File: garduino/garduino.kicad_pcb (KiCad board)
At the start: 2 copper layers, 65 x 56 mm, 62 parts, among them J1 Hum1, J10 OUT6, J11 DIN1, J12 OUT5, J13 OUT4, J14 OUT3, J15 isp, J16 OUT2, J17 OUT1, J18 RPi, J2 Hum2, J3 Hum3, J4 Hum4, J5 Hum5, J6 Hum6, J7 RL0, J8 OUT7, J9 DIN0, Q1 Q_PNP_BCE, Q2 Q_PNP_BCE, Q3 Q_PNP_BCE, Q4 Q_PNP_BCE, Q5 Q_PNP_BCE, Q6 Q_PNP_BCE, Q7 Q_PNP_BCE, Q8 Q_PNP_BCE, SW1 reset, U1 TPIC6595, U2 ATmega328-AU, U3 LM7805_TO220

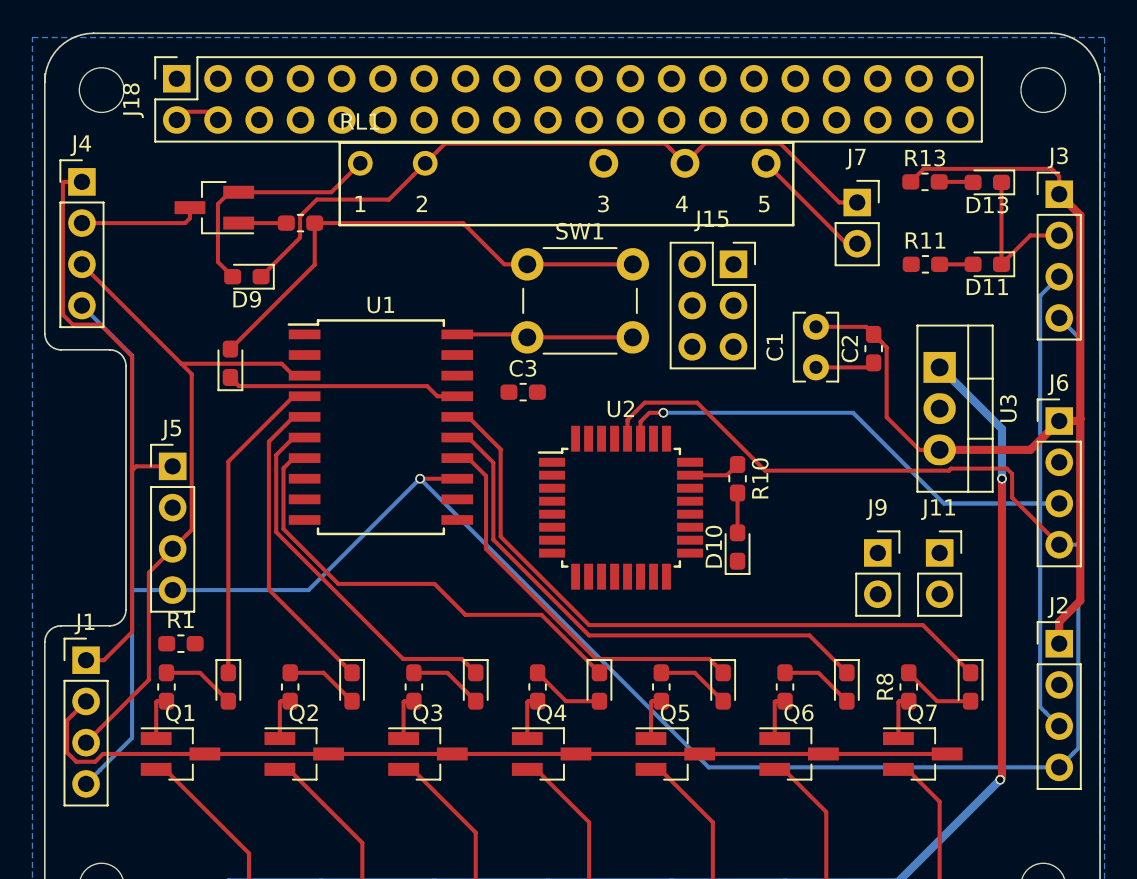
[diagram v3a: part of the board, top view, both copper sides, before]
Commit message: Add capsensor, humidity sensor p3, garduino with avr
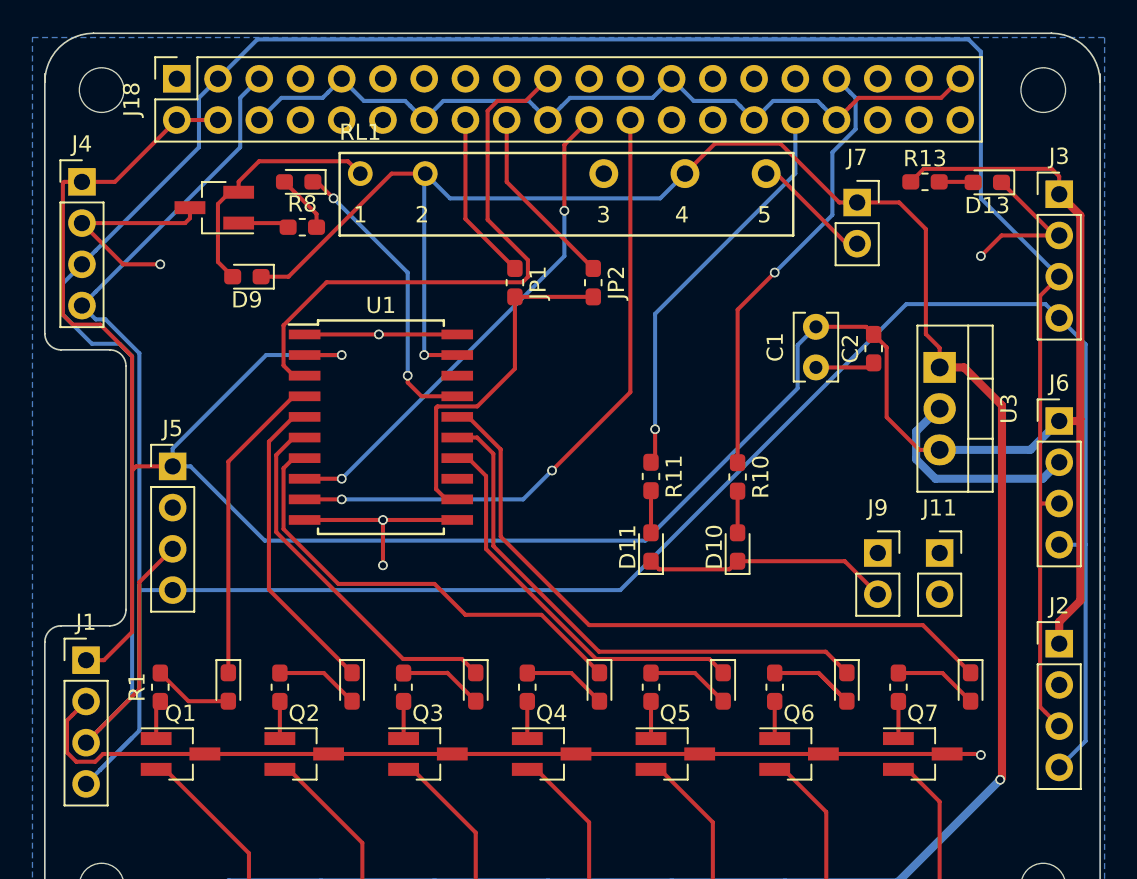
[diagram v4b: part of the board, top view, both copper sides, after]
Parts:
- removed C3: 100nF, Capacitor_SMD:C_0603_1608Metric_Pad1.05x0.95mm_HandSolder
- removed J15: isp, Connector_PinSocket_2.54mm:PinSocket_2x03_P2.54mm_Vertical
- removed R9: 10k, Resistor_SMD:R_0603_1608Metric_Pad1.05x0.95mm_HandSolder
- removed SW1: reset, Button_Switch_THT:SW_PUSH_6mm_H4.3mm
- removed U2: ATmega328-AU, Package_QFP:TQFP-32_7x7mm_P0.8mm
- added JP1: BCM23, Resistor_SMD:R_0603_1608Metric_Pad1.05x0.95mm_HandSolder, F.Cu at (118.6, 104.0)
- added JP2: BCM24, Resistor_SMD:R_0603_1608Metric_Pad1.05x0.95mm_HandSolder, F.Cu at (123.4, 104.0)
- moved R8 46.9 mm to (105.5, 100.6), turned to 0 degrees
- moved D11 27.1 mm to (127.0, 120.3), turned to 90 degrees
- moved R11 21.4 mm to (127.0, 115.9), turned to 270 degrees
- moved D8 11.9 mm to (105.3, 97.8), turned to 180 degrees
- moved R7 6.99 mm to (142.2, 128.9)
- moved R2 6.99 mm to (104.1, 128.9)
- moved R3 6.99 mm to (111.8, 128.9)
- moved R4 6.99 mm to (119.4, 128.9)
- moved R5 6.99 mm to (127.0, 128.9)
- moved R6 6.99 mm to (134.6, 128.9)
- moved R1 2.97 mm to (96.8, 128.9), turned to 90 degrees
- moved RL1 0.63 mm to (109.1, 97.3)
- moved R10 0.11 mm to (132.3, 116.0)
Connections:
- net /MOSI renamed /SPI0_MOSI
- J18 pad 16: (no net) -> /BCM23
- J18 pad 18: (no net) -> /BCM24
- J18 pad 2: /5v -> +5V
- J18 pad 21: /MISO -> (no net)
- J18 pad 22: (no net) -> /BCM25
- J18 pad 24: (no net) -> /SPI0_CE0
- J18 pad 3: /RESET -> /SDA
- J18 pad 32: (no net) -> /PWM0
- J18 pad 33: (no net) -> /PWM1
- J18 pad 4: /5v -> +5V
- J18 pad 5: (no net) -> /SCL
- J5 pad 3: (no net) -> /SDA
- R10 pad 1: /LED1 -> /PWM1
- R11 pad 1: /LED2 -> /PWM0
- U1 pad 13: /SCK -> (no net)
- U1 pad 8: /RESET -> /BCM25
- U1 pad 9: /G# -> /SPI0_CE0
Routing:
- net /SCK: track 131.4 -> 0.00 mm, vias 1 -> 0
- net /SCL: track 32.8 -> 148.0 mm
- net /SDA: track 58.0 -> 156.9 mm, vias 1 -> 0
- net GND: track 89.6 -> 188.3 mm, vias 0 -> 6
- net +5V: track 100.0 -> 174.7 mm, vias 0 -> 1
- net /SPI0_CE0: track 0.00 -> 39.6 mm, vias 0 -> 2
- net /BCM25: track 0.00 -> 30.7 mm, vias 0 -> 2
- net +12V: track 130.4 -> 157.8 mm
- net /PWM1: track 0.00 -> 27.1 mm, vias 0 -> 1
- net /PWM0: track 0.00 -> 24.8 mm, vias 0 -> 1
- net /RCLK: track 0.00 -> 21.7 mm
- net Net-(C3-Pad1): track 20.2 -> 0.00 mm
- net /BCM24: track 0.00 -> 11.4 mm
- net /BCM23: track 0.00 -> 10.4 mm
- net /SPI0_MOSI: track 42.9 -> 36.1 mm
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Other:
- board text removed: "Camera Flex Slot (Optional)"

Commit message: Garduino with FETs
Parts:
- removed D1, D10, D11, D13, D2, D3, D4, D5, D6, D7: LED, LED_SMD:LED_0603_1608Metric_Pad1.05x0.95mm_HandSolder
- removed the D8 at (105.3, 97.8)
- removed the J14 at (113.0, 142.2)
- removed JP1: BCM23, Resistor_SMD:R_0603_1608Metric_Pad1.05x0.95mm_HandSolder
- removed JP2: BCM24, Resistor_SMD:R_0603_1608Metric_Pad1.05x0.95mm_HandSolder
- removed R1, R3, R4, R5, R6, R7: 1k, Resistor_SMD:R_0603_1608Metric_Pad1.05x0.95mm_HandSolder
- removed R2: 10k, Resistor_SMD:R_0603_1608Metric_Pad1.05x0.95mm_HandSolder
- removed U1: TPIC6595, Package_SO:SOIC-20W_7.5x12.8mm_P1.27mm
- removed U3: LM7805_TO220, Package_TO_SOT_THT:TO-220-3_Vertical
- added C1: 100n, Capacitor_SMD:C_0603_1608Metric_Pad1.05x0.95mm_HandSolder, F.Cu at (123.3, 111.8)
- added C2: 22pF, Capacitor_SMD:C_0603_1608Metric_Pad1.05x0.95mm_HandSolder, F.Cu at (119.7, 111.8)
- added C3: 22pF, Capacitor_SMD:C_0603_1608Metric_Pad1.05x0.95mm_HandSolder, F.Cu at (116.2, 111.8)
- added D9: LED, LED_SMD:LED_0603_1608Metric_Pad1.05x0.95mm_HandSolder, F.Cu at (147.1, 142.6)
- added J15: OUT3, Connector_PinSocket_2.54mm:PinSocket_1x02_P2.54mm_Vertical, F.Cu at (114.6, 142.0)
- added J17: OUT2, Connector_PinSocket_2.54mm:PinSocket_1x02_P2.54mm_Vertical, F.Cu at (107.4, 142.0)
- added J9: ADC6, Connector_PinHeader_2.54mm:PinHeader_1x03_P2.54mm_Vertical, F.Cu at (147.6, 119.6)
- added Q10: BSS138, Package_TO_SOT_SMD:SOT-23, F.Cu at (93.9, 101.7)
- added Q11: BSS138, Package_TO_SOT_SMD:SOT-23, F.Cu at (133.1, 114.3)
- added Q12: NCV8403, Package_TO_SOT_SMD:TO-252-2, F.Cu at (104.0, 105.5)
- added Q9: BSS138, Package_TO_SOT_SMD:SOT-23, B.Cu at (123.3, 103.1)
- added R12: 10k, Resistor_SMD:R_0603_1608Metric_Pad1.05x0.95mm_HandSolder, F.Cu at (93.8, 98.4)
- added R14: 1k, Resistor_SMD:R_0603_1608Metric_Pad1.05x0.95mm_HandSolder, F.Cu at (147.1, 138.9)
- added R15: 10k, Resistor_SMD:R_0603_1608Metric_Pad1.05x0.95mm_HandSolder, F.Cu at (136.0, 114.3)
- added R16: 10k, Resistor_SMD:R_0603_1608Metric_Pad1.05x0.95mm_HandSolder, F.Cu at (130.2, 114.3)
- added R17: 10k, Resistor_SMD:R_0603_1608Metric_Pad1.05x0.95mm_HandSolder, B.Cu at (130.7, 106.6)
- added R9: 10k, Resistor_SMD:R_0603_1608Metric_Pad1.05x0.95mm_HandSolder, B.Cu at (118.1, 103.1)
- added SW1: SW_DIP_x01, Button_Switch_SMD:SW_SPST_B3S-1000, F.Cu at (130.5, 106.6)
- added U2: ATmega328P-AU, Package_QFP:TQFP-32_7x7mm_P0.8mm, F.Cu at (120.4, 118.5)
- added Y1: Crystal, Crystal:Crystal_HC18-U_Vertical, F.Cu at (121.9, 108.0)
- D8: renamed from D9; moved to B.Cu
- J1: value Hum1 -> ADC1; footprint Connector_PinHeader_2.54mm:PinHeader_1x04_P2.54mm_Vertical -> Connector_PinHeader_2.54mm:PinHeader_1x03_P2.54mm_Vertical
- J11: value DIN1 -> ADC7; footprint Connector_PinSocket_2.54mm:PinSocket_1x02_P2.54mm_Vertical -> Connector_PinHeader_2.54mm:PinHeader_1x03_P2.54mm_Vertical
- J14: renamed from J9; value DIN0 -> DIN
- J16: value OUT2 -> 12v
- J2: value Hum2 -> ADC2; footprint Connector_PinHeader_2.54mm:PinHeader_1x04_P2.54mm_Vertical -> Connector_PinHeader_2.54mm:PinHeader_1x03_P2.54mm_Vertical
- J3: value Hum3 -> ADC3; footprint Connector_PinHeader_2.54mm:PinHeader_1x04_P2.54mm_Vertical -> Connector_PinHeader_2.54mm:PinHeader_1x03_P2.54mm_Vertical
- J4: value Hum4 -> Max7219; footprint Connector_PinHeader_2.54mm:PinHeader_1x04_P2.54mm_Vertical -> Connector_PinHeader_2.54mm:PinHeader_1x05_P2.54mm_Vertical
- J5: value Hum5 -> ADC4; footprint Connector_PinHeader_2.54mm:PinHeader_1x04_P2.54mm_Vertical -> Connector_PinHeader_2.54mm:PinHeader_1x03_P2.54mm_Vertical
- J6: value Hum6 -> ADC5; footprint Connector_PinHeader_2.54mm:PinHeader_1x04_P2.54mm_Vertical -> Connector_PinHeader_2.54mm:PinHeader_1x03_P2.54mm_Vertical
- J7: value RL0 -> OUT8
- Q1, Q2, Q3, Q4, Q5, Q6, Q7: value Q_PNP_BCE -> NCV8403; footprint Package_TO_SOT_SMD:SOT-23_Handsoldering -> Package_TO_SOT_SMD:TO-252-2
- Q8: value Q_PNP_BCE -> BSS138; footprint Package_TO_SOT_SMD:SOT-23_Handsoldering -> Package_TO_SOT_SMD:SOT-23; moved to B.Cu
- R10, R11, R8: value 1k -> 10k; moved to B.Cu
- R13: value 1k -> 10k
- moved J1 66.1 mm to (151.9, 98.8)
- moved J5 56.3 mm to (151.9, 130.0)
- moved R13 50.5 mm to (93.8, 104.5)
- moved J14 22.8 mm to (147.6, 98.8)
- moved J3 21.1 mm to (151.9, 119.6)
- moved J4 18.8 mm to (104.4, 111.9)
- moved J6 18.1 mm to (147.6, 130.0)
- moved J16 17.8 mm to (92.2, 131.8), turned to 0 degrees
- moved R10 17.4 mm to (120.5, 103.1)
- moved J2 17.0 mm to (151.9, 109.2)
- moved Q8 15.6 mm to (115.2, 103.1), turned to 0 degrees
- moved R11 12.8 mm to (126.2, 103.1)
- moved J11 11.8 mm to (147.6, 109.2)
- moved D8 9.67 mm to (111.0, 99.8)
- moved R8 7.32 mm to (112.4, 103.1), turned to 270 degrees
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- renumbered C1 to C4, C2 to C5, J17 to J18, J18 to J19
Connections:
- J1 pad 1: +5V -> GND
- J1 pad 2: GND -> +5V
- J1 pad 3: /SDA -> /PC5
- J11 pad 1: (no net) -> GND
- J11 pad 2: GND -> +5V
- J14 pad 1: (no net) -> GND
- J14 pad 2: GND -> /PD4
- J16 pad 1: +12V -> GND
- J16 pad 2: /OUT1 -> +12V
- J19 pad 1: (no net) -> +3V3
- J19 pad 16: /BCM23 -> (no net)
- J19 pad 18: /BCM24 -> (no net)
- J19 pad 21: (no net) -> /SPI0_MISO
- J19 pad 23: (no net) -> /SPI0_SCLK
- J19 pad 24: /SPI0_CE0 -> (no net)
- J19 pad 3: /SDA -> (no net)
- J19 pad 32: /PWM0 -> (no net)
- J19 pad 33: /PWM1 -> (no net)
- J19 pad 5: /SCL -> (no net)
- J2 pad 1: +5V -> GND
- J2 pad 2: (no net) -> +5V
- J2 pad 3: /SDA -> /PC3
- J3 pad 1: +5V -> GND
- J3 pad 2: GND -> +5V
- J3 pad 3: /SDA -> /PC2
- J4 pad 3: /SDA -> /MAXDIN
- J4 pad 4: /SCL -> /MAXCS
- J5 pad 1: +5V -> GND
- J5 pad 2: GND -> +5V
- J5 pad 3: /SDA -> /ADC7
- J6 pad 1: +5V -> GND
- J6 pad 2: GND -> +5V
- J6 pad 3: /SDA -> /ADC6
- Q1 pad 1: Net-(Q1-Pad1) -> /PB0
- Q2 pad 1: Net-(Q2-Pad1) -> /PB1
- Q3 pad 1: Net-(Q3-Pad1) -> /PD0
- Q4 pad 1: Net-(Q4-Pad1) -> /PD1
- Q5 pad 1: Net-(Q5-Pad1) -> /PD2
- Q6 pad 1: Net-(Q6-Pad1) -> /PD3
- Q7 pad 1: Net-(Q7-Pad1) -> /PD4
- Q8 pad 1: Net-(Q8-Pad1) -> +3V3
- Q8 pad 2: /OUT7 -> /SPI0_MOSI
- Q8 pad 3: GND -> /MOSI
- R10 pad 1: /PWM1 -> /SPI0_MISO
- R10 pad 2: Net-(D10-Pad2) -> +3V3
- R11 pad 1: /PWM0 -> /MISO
- R11 pad 2: Net-(D11-Pad2) -> +5V
- R13 pad 1: +5V -> /SCLK
- R13 pad 2: Net-(D13-Pad2) -> +5V
- R8 pad 1: Net-(Q8-Pad1) -> /SPI0_MOSI
- R8 pad 2: Net-(D8-Pad2) -> +3V3
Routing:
- net /SDA: track 156.9 -> 0.00 mm
- net /SCL: track 148.0 -> 0.00 mm
- net GND: track 188.3 -> 288.8 mm, vias 6 -> 11
- net +3V3: track 0.00 -> 79.7 mm, vias 0 -> 2
- net /PD4: track 0.00 -> 62.5 mm, vias 0 -> 2
- net /SCLK: track 0.00 -> 44.6 mm
- net /SPI0_SCLK: track 0.00 -> 41.5 mm
- net /DRAIN6: track 41.3 -> 0.00 mm
- net /ADC7: track 0.00 -> 39.8 mm
- net /SPI0_CE0: track 39.6 -> 0.00 mm, vias 2 -> 0
- net /ADC6: track 0.00 -> 37.8 mm
- net /PC5: track 0.00 -> 33.5 mm
- net /DRAIN5: track 33.3 -> 0.00 mm
- net /PC3: track 0.00 -> 29.8 mm
- net /PB0: track 0.00 -> 29.6 mm, vias 0 -> 2
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- removed copper zone on B.Cu, net GND
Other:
- board text added: "+"

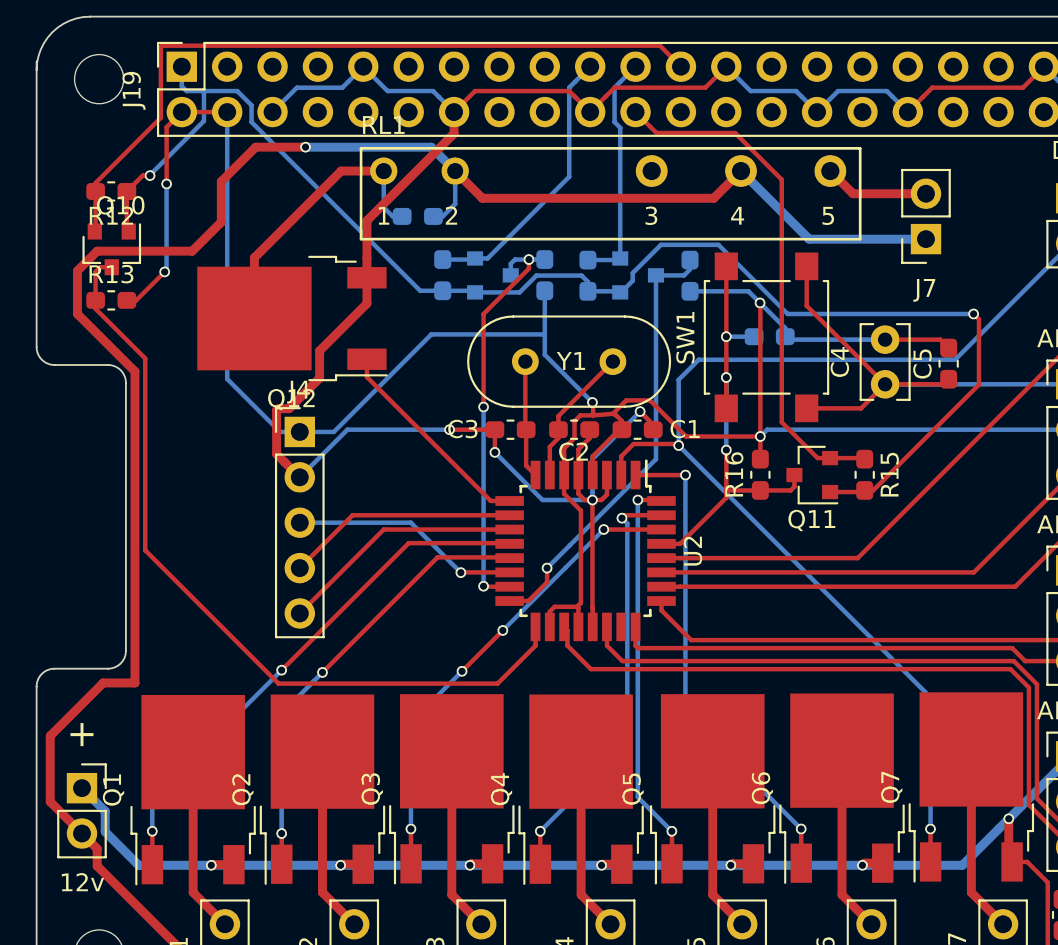
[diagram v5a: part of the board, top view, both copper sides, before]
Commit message: Remove hifiberry-adc-dac, garduino untested
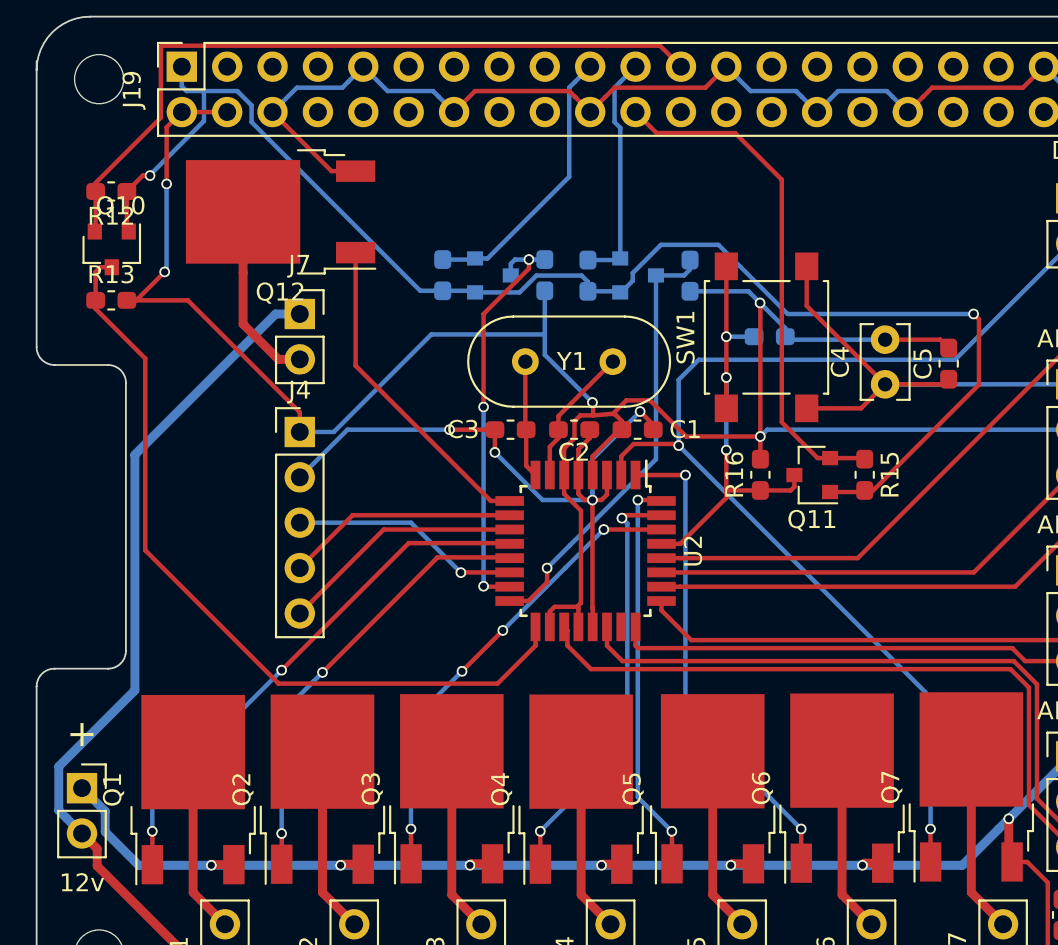
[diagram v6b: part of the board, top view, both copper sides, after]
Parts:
- removed D8: D, Diode_SMD:D_0603_1608Metric_Pad1.05x0.95mm_HandSolder
- removed RL1: FTR-LYCA, lci-kicad:FTR-LYCA
- moved J7 35.3 mm to (104.4, 105.3), turned to 0 degrees
- moved Q12 6.00 mm to (103.3, 99.6)
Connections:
- J7 pad 2: /RL0 -> /OUT7
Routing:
- net +12V: track 150.3 -> 91.3 mm, vias 1 -> 0
- net GND: track 288.8 -> 269.3 mm
- net +5V: track 188.9 -> 182.0 mm
- net /PD5: track 11.9 -> 18.1 mm
- net /RL0: track 5.88 -> 0.00 mm
- net /OUT7: track 15.9 -> 10.3 mm
